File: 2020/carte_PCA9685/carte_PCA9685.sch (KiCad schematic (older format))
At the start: 2 parts

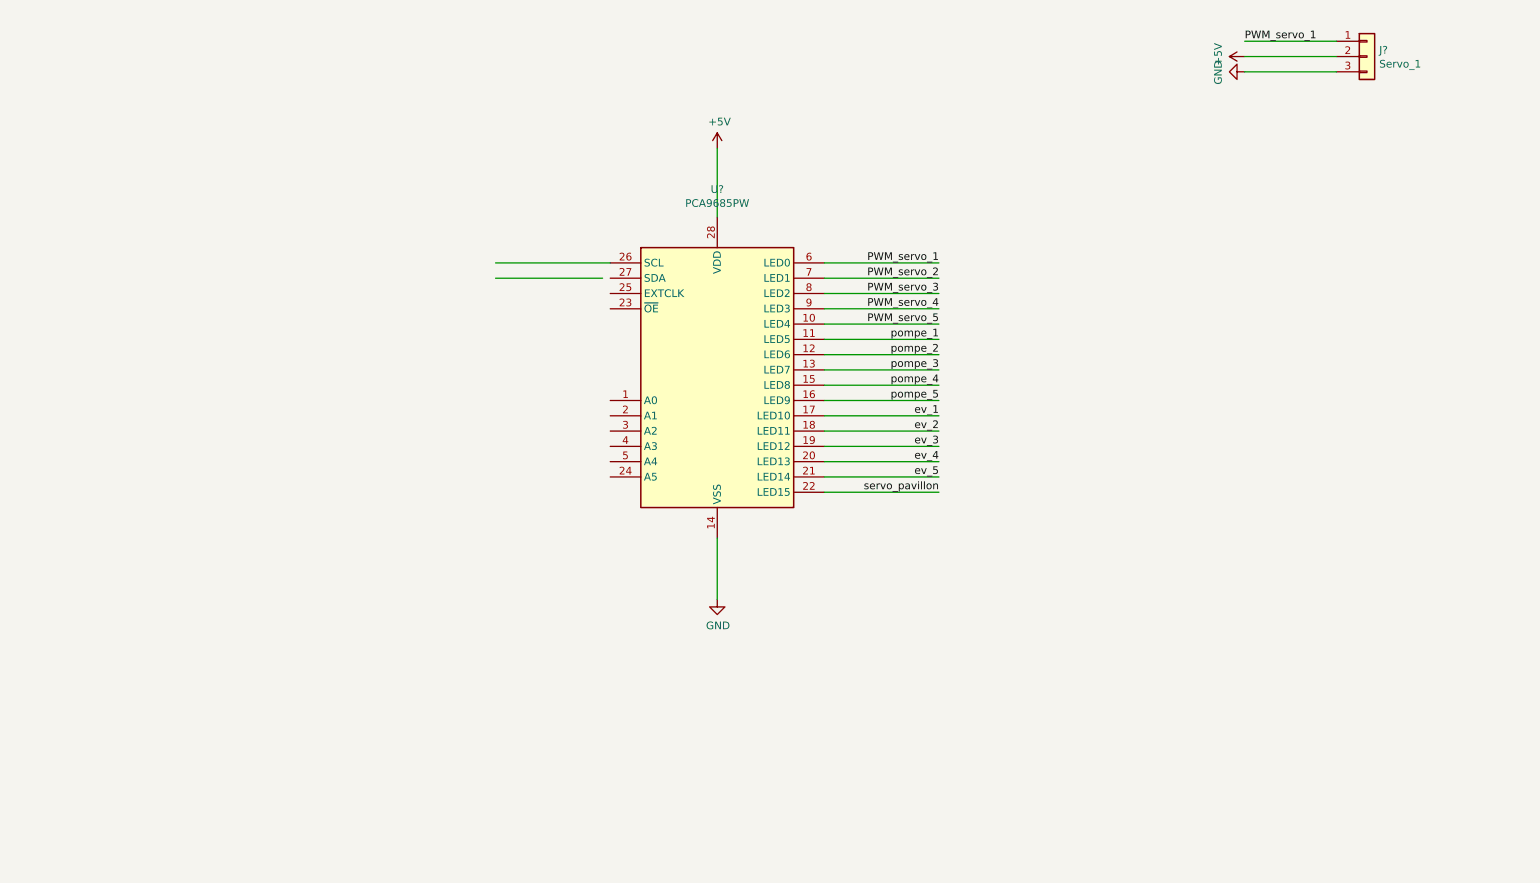
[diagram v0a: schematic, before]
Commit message: finish schematic PCA9685 and robotA
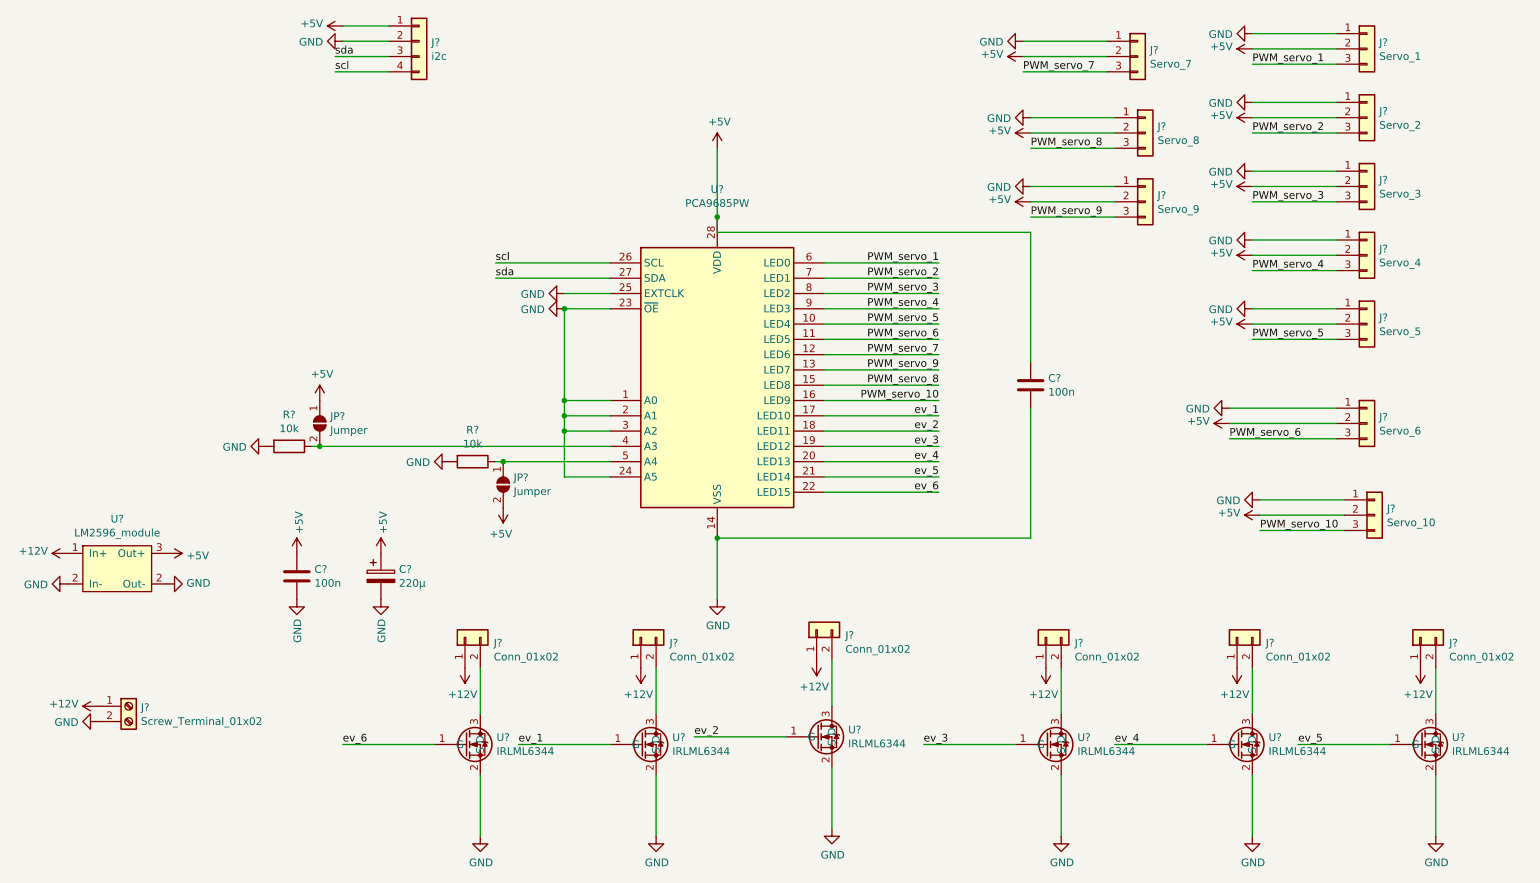
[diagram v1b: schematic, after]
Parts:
- added C? (x2): 100n, Capacitor_SMD:C_0603_1608Metric_Pad1.05x0.95mm_HandSolder, symbol Device:C
- added C?: 220µ, Capacitor_THT:CP_Radial_D10.0mm_P7.50mm, symbol Device:CP
- added J?: Screw_Terminal_01x02, TerminalBlock_4Ucon:TerminalBlock_4Ucon_1x02_P3.50mm_Vertical, symbol Connector:Screw_Terminal_01x02
- added J?: Servo_2, Connector_PinHeader_2.54mm:PinHeader_1x03_P2.54mm_Vertical, symbol Connector_Generic:Conn_01x03
- added J?: Servo_3, Connector_PinHeader_2.54mm:PinHeader_1x03_P2.54mm_Vertical, symbol Connector_Generic:Conn_01x03
- added J?: Servo_4, Connector_PinHeader_2.54mm:PinHeader_1x03_P2.54mm_Vertical, symbol Connector_Generic:Conn_01x03
- added J?: Servo_5, Connector_PinHeader_2.54mm:PinHeader_1x03_P2.54mm_Vertical, symbol Connector_Generic:Conn_01x03
- added J?: Servo_10, Connector_PinHeader_2.54mm:PinHeader_1x03_P2.54mm_Vertical, symbol Connector_Generic:Conn_01x03
- added J?: Servo_6, Connector_PinHeader_2.54mm:PinHeader_1x03_P2.54mm_Vertical, symbol Connector_Generic:Conn_01x03
- added J? (x6): Conn_01x02, Connector_JST:JST_XH_B2B-XH-A_1x02_P2.50mm_Vertical, symbol Connector_Generic:Conn_01x02
- added J?: Servo_7, Connector_PinHeader_2.54mm:PinHeader_1x03_P2.54mm_Vertical, symbol Connector_Generic:Conn_01x03
- added J?: Servo_8, Connector_PinHeader_2.54mm:PinHeader_1x03_P2.54mm_Vertical, symbol Connector_Generic:Conn_01x03
- added J?: Servo_9, Connector_PinHeader_2.54mm:PinHeader_1x03_P2.54mm_Vertical, symbol Connector_Generic:Conn_01x03
- added J?: i2c, symbol Connector_Generic:Conn_01x04
- added JP? (x2): Jumper, symbol Jumper:SolderJumper_2_Open
- added R? (x2): 10k, Resistor_SMD:R_0805_2012Metric, symbol Device:R
- added U?: LM2596_module, myFootprints:LM2596_module, symbol carte_PCA9685-rescue:LM2596_module-FBO-libs
- added U? (x6): IRLML6344, myFootprints:SOT-23, symbol carte_PCA9685-rescue:IRLML6344-FBO-libs
- J?: footprint (none) -> Connector_PinHeader_2.54mm:PinHeader_1x03_P2.54mm_Vertical
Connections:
- net labels added: +12V, PWM_servo_10, PWM_servo_6, PWM_servo_7, PWM_servo_8, PWM_servo_9, ev_6, scl, sda
- net labels removed: pompe_1, pompe_2, pompe_3, pompe_4, pompe_5, servo_pavillon
- wire segments 23 -> 91
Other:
- moved on the sheet: J?

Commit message: routing carte_PCA9685
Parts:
- J2: renamed from J?; footprint (none) -> Connector_JST:JST_XH_B4B-XH-A_1x04_P2.50mm_Vertical
- JP1, JP2: renamed from JP?; footprint (none) -> Jumper:SolderJumper-2_P1.3mm_Open_TrianglePad1.0x1.5mm
- gave numbers to parts that had none: 30

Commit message: Correction cartes 2020 robotA
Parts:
- J11, J12, J13, J14, J15, J16, J17, J7, J8, J9: footprint Connector_PinHeader_2.54mm:PinHeader_1x03_P2.54mm_Vertical -> Connector_JST:JST_EH_B3B-EH-A_1x03_P2.50mm_Vertical
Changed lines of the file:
@@
 F 0 "J11" H 10180 1142 50  0000 L CNN
 F 1 "Servo_1" H 10180 1051 50  0000 L CNN
-F 2 "Connector_PinHeader_2.54mm:PinHeader_1x03_P2.54mm_Vertical" H 10100 1100 50  0001 C CNN
+F 2 "Connector_JST:JST_EH_B3B-EH-A_1x03_P2.50mm_Vertical" H 10100 1100 50  0001 C CNN
 F 3 "~" H 10100 1100 50  0001 C CNN
 	1    10100 1100
@@
 F 0 "J12" H 10180 1592 50  0000 L CNN
 F 1 "Servo_2" H 10180 1501 50  0000 L CNN
-F 2 "Connector_PinHeader_2.54mm:PinHeader_1x03_P2.54mm_Vertical" H 10100 1550 50  0001 C CNN
+F 2 "Connector_JST:JST_EH_B3B-EH-A_1x03_P2.50mm_Vertical" H 10100 1550 50  0001 C CNN
 F 3 "~" H 10100 1550 50  0001 C CNN
 	1    10100 1550
@@
 F 0 "J13" H 10180 2042 50  0000 L CNN
 F 1 "Servo_3" H 10180 1951 50  0000 L CNN
-F 2 "Connector_PinHeader_2.54mm:PinHeader_1x03_P2.54mm_Vertical" H 10100 2000 50  0001 C CNN
+F 2 "Connector_JST:JST_EH_B3B-EH-A_1x03_P2.50mm_Vertical" H 10100 2000 50  0001 C CNN
 F 3 "~" H 10100 2000 50  0001 C CNN
 	1    10100 2000
@@
 F 0 "J14" H 10180 2492 50  0000 L CNN
 F 1 "Servo_4" H 10180 2401 50  0000 L CNN
-F 2 "Connector_PinHeader_2.54mm:PinHeader_1x03_P2.54mm_Vertical" H 10100 2450 50  0001 C CNN
+F 2 "Connector_JST:JST_EH_B3B-EH-A_1x03_P2.50mm_Vertical" H 10100 2450 50  0001 C CNN
 F 3 "~" H 10100 2450 50  0001 C CNN
 	1    10100 2450
@@
 F 0 "J15" H 10180 2942 50  0000 L CNN
 F 1 "Servo_5" H 10180 2851 50  0000 L CNN
-F 2 "Connector_PinHeader_2.54mm:PinHeader_1x03_P2.54mm_Vertical" H 10100 2900 50  0001 C CNN
+F 2 "Connector_JST:JST_EH_B3B-EH-A_1x03_P2.50mm_Vertical" H 10100 2900 50  0001 C CNN
 F 3 "~" H 10100 2900 50  0001 C CNN
 	1    10100 2900
@@
 F 0 "J17" H 10230 4192 50  0000 L CNN
 F 1 "Servo_10" H 10230 4101 50  0000 L CNN
-F 2 "Connector_PinHeader_2.54mm:PinHeader_1x03_P2.54mm_Vertical" H 10150 4150 50  0001 C CNN
+F 2 "Connector_JST:JST_EH_B3B-EH-A_1x03_P2.50mm_Vertical" H 10150 4150 50  0001 C CNN
 F 3 "~" H 10150 4150 50  0001 C CNN
 	1    10150 4150
@@
 F 0 "J16" H 10180 3592 50  0000 L CNN
 F 1 "Servo_6" H 10180 3501 50  0000 L CNN
-F 2 "Connector_PinHeader_2.54mm:PinHeader_1x03_P2.54mm_Vertical" H 10100 3550 50  0001 C CNN
+F 2 "Connector_JST:JST_EH_B3B-EH-A_1x03_P2.50mm_Vertical" H 10100 3550 50  0001 C CNN
 F 3 "~" H 10100 3550 50  0001 C CNN
 	1    10100 3550
@@
 F 0 "J7" H 8680 1192 50  0000 L CNN
 F 1 "Servo_7" H 8680 1101 50  0000 L CNN
-F 2 "Connector_PinHeader_2.54mm:PinHeader_1x03_P2.54mm_Vertical" H 8600 1150 50  0001 C CNN
+F 2 "Connector_JST:JST_EH_B3B-EH-A_1x03_P2.50mm_Vertical" H 8600 1150 50  0001 C CNN
 F 3 "~" H 8600 1150 50  0001 C CNN
 	1    8600 1150
@@
 F 0 "J8" H 8730 1692 50  0000 L CNN
 F 1 "Servo_8" H 8730 1601 50  0000 L CNN
-F 2 "Connector_PinHeader_2.54mm:PinHeader_1x03_P2.54mm_Vertical" H 8650 1650 50  0001 C CNN
+F 2 "Connector_JST:JST_EH_B3B-EH-A_1x03_P2.50mm_Vertical" H 8650 1650 50  0001 C CNN
 F 3 "~" H 8650 1650 50  0001 C CNN
 	1    8650 1650
@@
 F 0 "J9" H 8730 2142 50  0000 L CNN
 F 1 "Servo_9" H 8730 2051 50  0000 L CNN
-F 2 "Connector_PinHeader_2.54mm:PinHeader_1x03_P2.54mm_Vertical" H 8650 2100 50  0001 C CNN
+F 2 "Connector_JST:JST_EH_B3B-EH-A_1x03_P2.50mm_Vertical" H 8650 2100 50  0001 C CNN
 F 3 "~" H 8650 2100 50  0001 C CNN
 	1    8650 2100

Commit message: Fin carte elec 2020 robot-a
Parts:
- I2C1: renamed from J2; value i2c -> Conn_01x04
- Servo_1: renamed from J11; value Servo_1 -> Conn_01x03; footprint Connector_JST:JST_EH_B3B-EH-A_1x03_P2.50mm_Vertical -> Connector_PinHeader_2.54mm:PinHeader_1x03_P2.54mm_Vertical
- Servo_10: renamed from J17; value Servo_10 -> Conn_01x03; footprint Connector_JST:JST_EH_B3B-EH-A_1x03_P2.50mm_Vertical -> Connector_PinHeader_2.54mm:PinHeader_1x03_P2.54mm_Vertical
- Servo_2: renamed from J12; value Servo_2 -> Conn_01x03; footprint Connector_JST:JST_EH_B3B-EH-A_1x03_P2.50mm_Vertical -> Connector_PinHeader_2.54mm:PinHeader_1x03_P2.54mm_Vertical
- Servo_3: renamed from J13; value Servo_3 -> Conn_01x03; footprint Connector_JST:JST_EH_B3B-EH-A_1x03_P2.50mm_Vertical -> Connector_PinHeader_2.54mm:PinHeader_1x03_P2.54mm_Vertical
- Servo_4: renamed from J14; value Servo_4 -> Conn_01x03; footprint Connector_JST:JST_EH_B3B-EH-A_1x03_P2.50mm_Vertical -> Connector_PinHeader_2.54mm:PinHeader_1x03_P2.54mm_Vertical
- Servo_5: renamed from J15; value Servo_5 -> Conn_01x03; footprint Connector_JST:JST_EH_B3B-EH-A_1x03_P2.50mm_Vertical -> Connector_PinHeader_2.54mm:PinHeader_1x03_P2.54mm_Vertical
- Servo_6: renamed from J16; value Servo_6 -> Conn_01x03; footprint Connector_JST:JST_EH_B3B-EH-A_1x03_P2.50mm_Vertical -> Connector_PinHeader_2.54mm:PinHeader_1x03_P2.54mm_Vertical
- Servo_7: renamed from J7; value Servo_7 -> Conn_01x03; footprint Connector_JST:JST_EH_B3B-EH-A_1x03_P2.50mm_Vertical -> Connector_PinHeader_2.54mm:PinHeader_1x03_P2.54mm_Vertical
- Servo_8: renamed from J8; value Servo_8 -> Conn_01x03; footprint Connector_JST:JST_EH_B3B-EH-A_1x03_P2.50mm_Vertical -> Connector_PinHeader_2.54mm:PinHeader_1x03_P2.54mm_Vertical
- Servo_9: renamed from J9; value Servo_9 -> Conn_01x03; footprint Connector_JST:JST_EH_B3B-EH-A_1x03_P2.50mm_Vertical -> Connector_PinHeader_2.54mm:PinHeader_1x03_P2.54mm_Vertical
- renumbered J4 to Ev_1, J5 to Ev_2, J6 to Ev_3, J10 to Ev_4, J18 to Ev_5, J3 to Ev_6
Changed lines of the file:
@@
 ev_6
 $Comp
-L Connector_Generic:Conn_01x03 J11
+L Connector_Generic:Conn_01x03 Servo_1
 U 1 1 5E4DC2C0
 P 10100 1100
-F 0 "J11" H 10180 1142 50  0000 L CNN
-F 1 "Servo_1" H 10180 1051 50  0000 L CNN
-F 2 "Connector_JST:JST_EH_B3B-EH-A_1x03_P2.50mm_Vertical" H 10100 1100 50  0001 C CNN
+F 0 "Servo_1" H 10180 1142 50  0000 L CNN
+F 1 "Conn_01x03" H 10180 1051 50  0000 L CNN
+F 2 "Connector_PinHeader_2.54mm:PinHeader_1x03_P2.54mm_Vertical" H 10100 1100 50  0001 C CNN
 F 3 "~" H 10100 1100 50  0001 C CNN
 	1    10100 1100
@@
 PWM_servo_1
 $Comp
-L Connector_Generic:Conn_01x03 J12
+L Connector_Generic:Conn_01x03 Servo_2
 U 1 1 5E591485
 P 10100 1550
-F 0 "J12" H 10180 1592 50  0000 L CNN
-F 1 "Servo_2" H 10180 1501 50  0000 L CNN
-F 2 "Connector_JST:JST_EH_B3B-EH-A_1x03_P2.50mm_Vertical" H 10100 1550 50  0001 C CNN
+F 0 "Servo_2" H 10180 1592 50  0000 L CNN
+F 1 "Conn_01x03" H 10180 1501 50  0000 L CNN
+F 2 "Connector_PinHeader_2.54mm:PinHeader_1x03_P2.54mm_Vertical" H 10100 1550 50  0001 C CNN
 F 3 "~" H 10100 1550 50  0001 C CNN
 	1    10100 1550
@@
 $EndComp
 $Comp
-L Connector_Generic:Conn_01x03 J13
+L Connector_Generic:Conn_01x03 Servo_3
 U 1 1 5E591C68
 P 10100 2000
-F 0 "J13" H 10180 2042 50  0000 L CNN
-F 1 "Servo_3" H 10180 1951 50  0000 L CNN
-F 2 "Connector_JST:JST_EH_B3B-EH-A_1x03_P2.50mm_Vertical" H 10100 2000 50  0001 C CNN
+F 0 "Servo_3" H 10180 2042 50  0000 L CNN
+F 1 "Conn_01x03" H 10180 1951 50  0000 L CNN
+F 2 "Connector_PinHeader_2.54mm:PinHeader_1x03_P2.54mm_Vertical" H 10100 2000 50  0001 C CNN
 F 3 "~" H 10100 2000 50  0001 C CNN
 	1    10100 2000
@@
 PWM_servo_3
 $Comp
-L Connector_Generic:Conn_01x03 J14
+L Connector_Generic:Conn_01x03 Servo_4
 U 1 1 5E592690
 P 10100 2450
-F 0 "J14" H 10180 2492 50  0000 L CNN
-F 1 "Servo_4" H 10180 2401 50  0000 L CNN
-F 2 "Connector_JST:JST_EH_B3B-EH-A_1x03_P2.50mm_Vertical" H 10100 2450 50  0001 C CNN
+F 0 "Servo_4" H 10180 2492 50  0000 L CNN
+F 1 "Conn_01x03" H 10180 2401 50  0000 L CNN
+F 2 "Connector_PinHeader_2.54mm:PinHeader_1x03_P2.54mm_Vertical" H 10100 2450 50  0001 C CNN
 F 3 "~" H 10100 2450 50  0001 C CNN
 	1    10100 2450
@@
 PWM_servo_4
 $Comp
-L Connector_Generic:Conn_01x03 J15
+L Connector_Generic:Conn_01x03 Servo_5
 U 1 1 5E5934AF
 P 10100 2900
-F 0 "J15" H 10180 2942 50  0000 L CNN
-F 1 "Servo_5" H 10180 2851 50  0000 L CNN
-F 2 "Connector_JST:JST_EH_B3B-EH-A_1x03_P2.50mm_Vertical" H 10100 2900 50  0001 C CNN
+F 0 "Servo_5" H 10180 2942 50  0000 L CNN
+F 1 "Conn_01x03" H 10180 2851 50  0000 L CNN
+F 2 "Connector_PinHeader_2.54mm:PinHeader_1x03_P2.54mm_Vertical" H 10100 2900 50  0001 C CNN
 F 3 "~" H 10100 2900 50  0001 C CNN
 	1    10100 2900
@@
 PWM_servo_2
 $Comp
-L Connector_Generic:Conn_01x03 J17
+L Connector_Generic:Conn_01x03 Servo_10
 U 1 1 5E596CCA
 P 10150 4150
-F 0 "J17" H 10230 4192 50  0000 L CNN
-F 1 "Servo_10" H 10230 4101 50  0000 L CNN
-F 2 "Connector_JST:JST_EH_B3B-EH-A_1x03_P2.50mm_Vertical" H 10150 4150 50  0001 C CNN
+F 0 "Servo_10" H 10230 4192 50  0000 L CNN
+F 1 "Conn_01x03" H 10230 4101 50  0000 L CNN
+F 2 "Connector_PinHeader_2.54mm:PinHeader_1x03_P2.54mm_Vertical" H 10150 4150 50  0001 C CNN
 F 3 "~" H 10150 4150 50  0001 C CNN
 	1    10150 4150
@@
 	4400 2600 5150 2600
 $Comp
-L Connector_Generic:Conn_01x03 J16
+L Connector_Generic:Conn_01x03 Servo_6
 U 1 1 5E5A372B
 P 10100 3550
-F 0 "J16" H 10180 3592 50  0000 L CNN
-F 1 "Servo_6" H 10180 3501 50  0000 L CNN
-F 2 "Connector_JST:JST_EH_B3B-EH-A_1x03_P2.50mm_Vertical" H 10100 3550 50  0001 C CNN
+F 0 "Servo_6" H 10180 3592 50  0000 L CNN
+F 1 "Conn_01x03" H 10180 3501 50  0000 L CNN
+F 2 "Connector_PinHeader_2.54mm:PinHeader_1x03_P2.54mm_Vertical" H 10100 3550 50  0001 C CNN
 F 3 "~" H 10100 3550 50  0001 C CNN
 	1    10100 3550
@@
 $EndComp
 $Comp
-L Connector_Generic:Conn_01x02 J5
+L Connector_Generic:Conn_01x02 Ev_2
 U 1 1 5E71409B
 P 6500 4900
-F 0 "J5" V 6464 4712 50  0000 R CNN
+F 0 "Ev_2" V 6464 4712 50  0000 R CNN
 F 1 "Conn_01x02" V 6373 4712 50  0000 R CNN
 F 2 "Connector_JST:JST_XH_B2B-XH-A_1x02_P2.50mm_Vertical" H 6500 4900 50  0001 C CNN
@@
 $EndComp
 $Comp
-L Connector_Generic:Conn_01x02 J6
+L Connector_Generic:Conn_01x02 Ev_3
 U 1 1 5E72FE37
 P 8000 4950
-F 0 "J6" V 7964 4762 50  0000 R CNN
+F 0 "Ev_3" V 7964 4762 50  0000 R CNN
 F 1 "Conn_01x02" V 7873 4762 50  0000 R CNN
 F 2 "Connector_JST:JST_XH_B2B-XH-A_1x02_P2.50mm_Vertical" H 8000 4950 50  0001 C CNN
@@
 $EndComp
 $Comp
-L Connector_Generic:Conn_01x02 J10
+L Connector_Generic:Conn_01x02 Ev_4
 U 1 1 5E7321AC
 P 9250 4950
-F 0 "J10" V 9214 4762 50  0000 R CNN
+F 0 "Ev_4" V 9214 4762 50  0000 R CNN
 F 1 "Conn_01x02" V 9123 4762 50  0000 R CNN
 F 2 "Connector_JST:JST_XH_B2B-XH-A_1x02_P2.50mm_Vertical" H 9250 4950 50  0001 C CNN
@@
 $EndComp
 $Comp
-L Connector_Generic:Conn_01x02 J18
+L Connector_Generic:Conn_01x02 Ev_5
 U 1 1 5E73476F
 P 10450 4950
-F 0 "J18" V 10414 4762 50  0000 R CNN
+F 0 "Ev_5" V 10414 4762 50  0000 R CNN
 F 1 "Conn_01x02" V 10323 4762 50  0000 R CNN
 F 2 "Connector_JST:JST_XH_B2B-XH-A_1x02_P2.50mm_Vertical" H 10450 4950 50  0001 C CNN
@@
 $EndComp
 $Comp
-L Connector_Generic:Conn_01x02 J4
+L Connector_Generic:Conn_01x02 Ev_1
 U 1 1 5E736984
 P 5350 4950
-F 0 "J4" V 5314 4762 50  0000 R CNN
+F 0 "Ev_1" V 5314 4762 50  0000 R CNN
 F 1 "Conn_01x02" V 5223 4762 50  0000 R CNN
 F 2 "Connector_JST:JST_XH_B2B-XH-A_1x02_P2.50mm_Vertical" H 5350 4950 50  0001 C CNN
@@
 $EndComp
 $Comp
-L Connector_Generic:Conn_01x02 J3
+L Connector_Generic:Conn_01x02 Ev_6
 U 1 1 5E73A269
 P 4200 4950
-F 0 "J3" V 4164 4762 50  0000 R CNN
+F 0 "Ev_6" V 4164 4762 50  0000 R CNN
 F 1 "Conn_01x02" V 4073 4762 50  0000 R CNN
 F 2 "Connector_JST:JST_XH_B2B-XH-A_1x02_P2.50mm_Vertical" H 4200 4950 50  0001 C CNN
@@
 $EndComp
 $Comp
-L Connector_Generic:Conn_01x03 J7
+L Connector_Generic:Conn_01x03 Servo_7
 U 1 1 5E760592
 P 8600 1150
-F 0 "J7" H 8680 1192 50  0000 L CNN
-F 1 "Servo_7" H 8680 1101 50  0000 L CNN
-F 2 "Connector_JST:JST_EH_B3B-EH-A_1x03_P2.50mm_Vertical" H 8600 1150 50  0001 C CNN
+F 0 "Servo_7" H 8680 1192 50  0000 L CNN
+F 1 "Conn_01x03" H 8680 1101 50  0000 L CNN
+F 2 "Connector_PinHeader_2.54mm:PinHeader_1x03_P2.54mm_Vertical" H 8600 1150 50  0001 C CNN
 F 3 "~" H 8600 1150 50  0001 C CNN
 	1    8600 1150
@@
 PWM_servo_7
 $Comp
-L Connector_Generic:Conn_01x03 J8
+L Connector_Generic:Conn_01x03 Servo_8
 U 1 1 5E761F8A
 P 8650 1650
-F 0 "J8" H 8730 1692 50  0000 L CNN
-F 1 "Servo_8" H 8730 1601 50  0000 L CNN
-F 2 "Connector_JST:JST_EH_B3B-EH-A_1x03_P2.50mm_Vertical" H 8650 1650 50  0001 C CNN
+F 0 "Servo_8" H 8730 1692 50  0000 L CNN
+F 1 "Conn_01x03" H 8730 1601 50  0000 L CNN
+F 2 "Connector_PinHeader_2.54mm:PinHeader_1x03_P2.54mm_Vertical" H 8650 1650 50  0001 C CNN
 F 3 "~" H 8650 1650 50  0001 C CNN
 	1    8650 1650
@@
 PWM_servo_8
 $Comp
-L Connector_Generic:Conn_01x03 J9
+L Connector_Generic:Conn_01x03 Servo_9
 U 1 1 5E7640D4
 P 8650 2100
-F 0 "J9" H 8730 2142 50  0000 L CNN
-F 1 "Servo_9" H 8730 2051 50  0000 L CNN
-F 2 "Connector_JST:JST_EH_B3B-EH-A_1x03_P2.50mm_Vertical" H 8650 2100 50  0001 C CNN
+F 0 "Servo_9" H 8730 2142 50  0000 L CNN
+F 1 "Conn_01x03" H 8730 2051 50  0000 L CNN
+F 2 "Connector_PinHeader_2.54mm:PinHeader_1x03_P2.54mm_Vertical" H 8650 2100 50  0001 C CNN
 F 3 "~" H 8650 2100 50  0001 C CNN
 	1    8650 2100
@@
 PWM_servo_9
 $Comp
-L Connector_Generic:Conn_01x04 J2
+L Connector_Generic:Conn_01x04 I2C1
 U 1 1 5E779B02
 P 3900 1050
-F 0 "J2" H 3980 1042 50  0000 L CNN
-F 1 "i2c" H 3980 951 50  0000 L CNN
+F 0 "I2C1" H 3980 1042 50  0000 L CNN
+F 1 "Conn_01x04" H 3980 951 50  0000 L CNN
 F 2 "Connector_JST:JST_XH_B4B-XH-A_1x04_P2.50mm_Vertical" H 3900 1050 50  0001 C CNN
 F 3 "~" H 3900 1050 50  0001 C CNN
